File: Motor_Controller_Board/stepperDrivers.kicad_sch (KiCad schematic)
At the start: 17 parts, among them J401 Conn_01x04

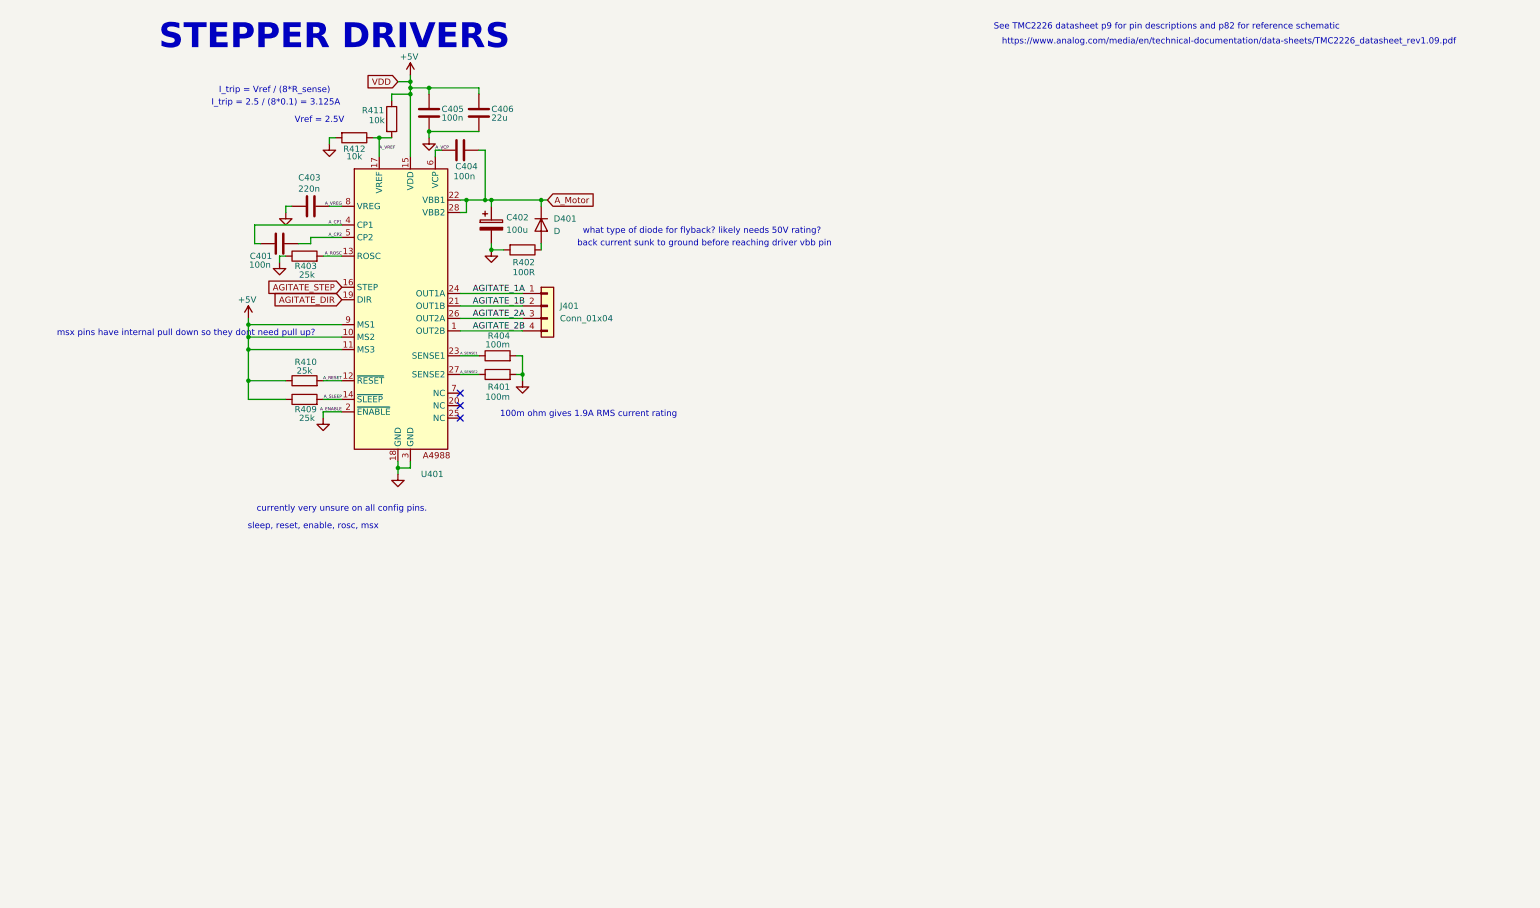
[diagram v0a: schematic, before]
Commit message: picking footprints. still need buck regulator footprints
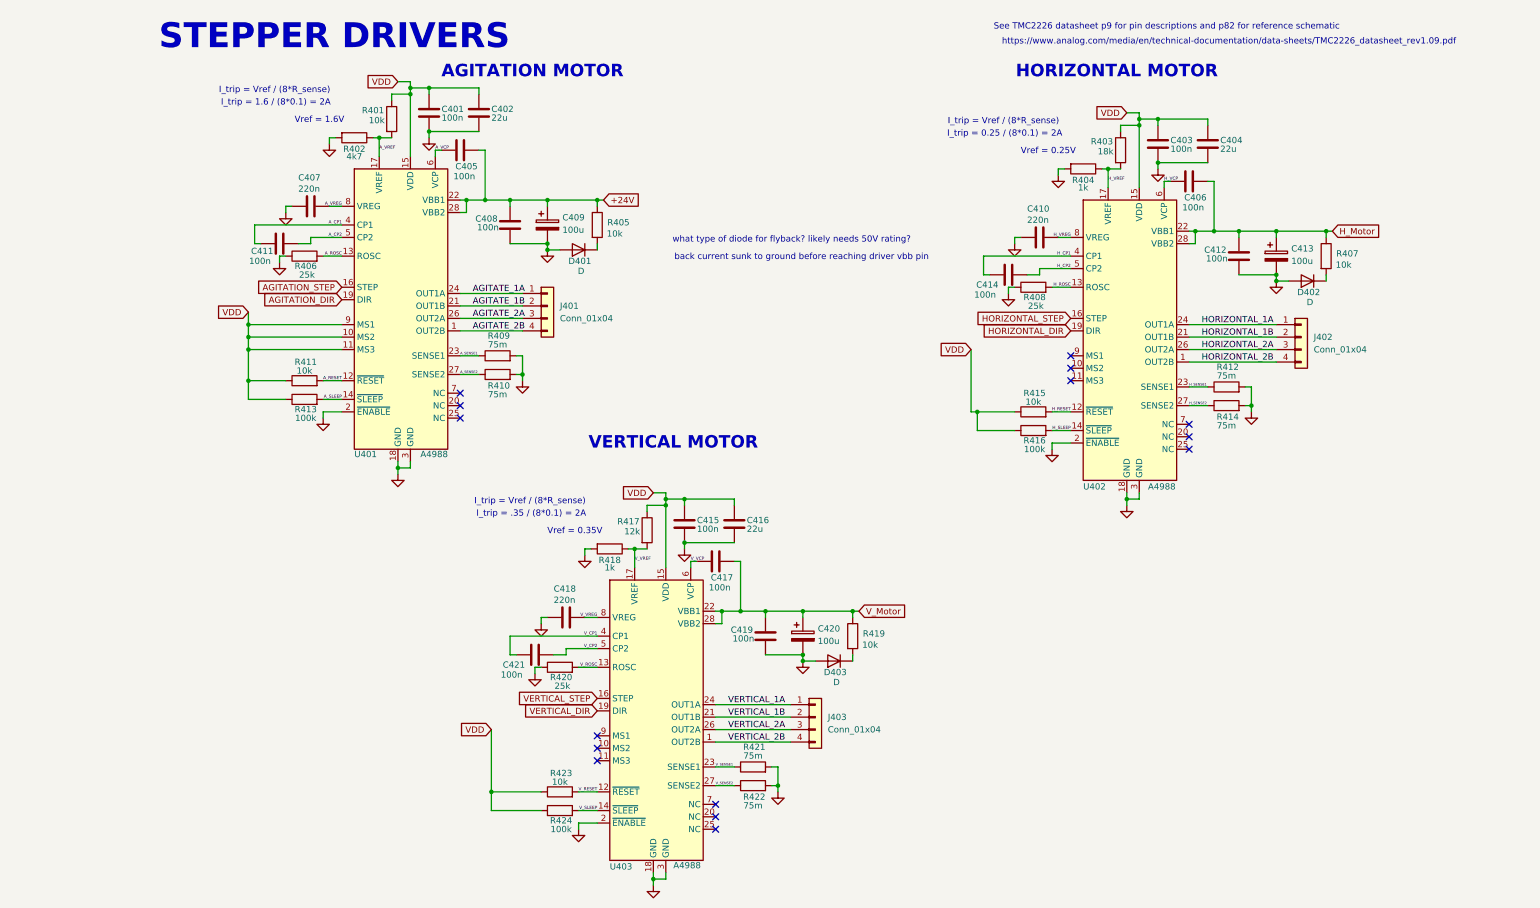
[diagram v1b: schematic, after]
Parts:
- removed C401: 100n, symbol Device:C
- removed R401: 100m, symbol Device:R
- added C404, C416: 22u, Capacitor_SMD:C_0603_1608Metric, symbol Device:C
- added C406, C408, C411, C412, C414, C415, C417, C419, C421: 100n, Capacitor_SMD:C_0603_1608Metric, symbol Device:C
- added C407, C410, C418: 220n, Capacitor_SMD:C_0805_2012Metric, symbol Device:C
- added C413, C420: 100u, Capacitor_THT:CP_Radial_D16.0mm_P7.50mm, symbol Device:C_Polarized
- added D402, D403: D, symbol Device:D
- added J402, J403: Conn_01x04, TerminalBlock:TerminalBlock_bornier-4_P5.08mm, symbol Connector_Generic:Conn_01x04
- added R403: 18k, Resistor_SMD:R_0603_1608Metric, symbol Device:R
- added R407, R415, R419, R423: 10k, Resistor_SMD:R_0603_1608Metric, symbol Device:R
- added R408, R420: 25k, Resistor_SMD:R_0603_1608Metric, symbol Device:R
- added R409, R410, R412, R414, R421, R422: 75m, Resistor_SMD:R_1206_3216Metric, symbol Device:R
- added R416, R424: 100k, Resistor_SMD:R_0603_1608Metric, symbol Device:R
- added R417: 12k, Resistor_SMD:R_0603_1608Metric, symbol Device:R
- added R418: 1k, Resistor_SMD:R_0603_1608Metric, symbol Device:R
- added U402, U403: A4988, Package_DFN_QFN:QFN-28-1EP_5x5mm_P0.5mm_EP3.25x3.25mm_ThermalVias, symbol a4988_symbol:A4988
- C401: renamed from C405; footprint (none) -> Capacitor_SMD:C_0603_1608Metric
- C402: renamed from C406; footprint (none) -> Capacitor_SMD:C_0603_1608Metric
- C403: value 220n -> 100n; footprint (none) -> Capacitor_SMD:C_0603_1608Metric
- C405: renamed from C404; footprint (none) -> Capacitor_SMD:C_0603_1608Metric; LCSC Part Number (none) -> C14663; MPN (none) -> CC0603KRX7R9BB104; Manufacturer (none) -> YAGEO
- C409: renamed from C402; footprint (none) -> Capacitor_THT:CP_Radial_D16.0mm_P7.50mm
- J401: footprint (none) -> TerminalBlock:TerminalBlock_bornier-4_P5.08mm
- R401: renamed from R411; footprint (none) -> Resistor_SMD:R_0603_1608Metric
- R402: renamed from R412; value 10k -> 4k7; footprint (none) -> Resistor_SMD:R_0603_1608Metric
- R404: value 100m -> 1k; footprint (none) -> Resistor_SMD:R_0603_1608Metric
- R405: renamed from R402; value 100R -> 10k; footprint (none) -> Resistor_SMD:R_0603_1608Metric
- R406: renamed from R403; footprint (none) -> Resistor_SMD:R_0603_1608Metric
- R411: renamed from R410; value 25k -> 10k; footprint (none) -> Resistor_SMD:R_0603_1608Metric
- R413: renamed from R409; value 25k -> 100k; footprint (none) -> Resistor_SMD:R_0603_1608Metric
- U401: value ~ -> A4988; footprint (none) -> Package_DFN_QFN:QFN-28-1EP_5x5mm_P0.5mm_EP3.25x3.25mm_ThermalVias
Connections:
- net A_CP1: now also C411.1
- net A_CP2: now also C411.2
- net A_SENSE1: now also R409.1; no longer R404.1
- net A_SENSE2: now also R410.1
- net A_VREG: now also C407.1; no longer C403.1
- net GND: now also D401.2 (A), C404.2, C407.2, C408.1, C410.2, C412.1, C413.2, C415.2, C416.2, C418.2, C419.1, C420.2, D402.2 (A), D403.2 (A), R408.1, R409.2, R410.2, R412.2, R414.2, R418.2, R420.1, R421.2, R422.2, U402.18 (GND), U402.2 (~{ENABLE}), U402.3 (GND), U403.18 (GND), U403.2 (~{ENABLE}), U403.3 (GND); no longer R405.2
- net +24V: now reaches R405.1
- net +24V: now also C405.2, C409.1, U401.22 (VBB1), U401.28 (VBB2), C408.2; no longer D401.2 (A)
- net +5V renamed VDD
- net VDD: now also C403.1, C404.1, C415.1, C416.1, R403.1, R415.1, R416.1, R417.1, R423.1, R424.1, U402.15 (VDD), U403.15 (VDD)
- net AGITATE_DIR renamed AGITATION_DIR
- net AGITATE_STEP renamed AGITATION_STEP
- removed net A_Motor: C405.2, C409.1, D401.1 (K), U401.22 (VBB1), U401.28 (VBB2)
- new net: D403.1 (K), R419.2
- new net: D401.1 (K), R405.2
- new net: D402.1 (K), R407.2
- new net HORIZONTAL_1A: J402.1 (Pin_1), U402.24 (OUT1A)
- new net HORIZONTAL_1B: J402.2 (Pin_2), U402.21 (OUT1B)
- new net HORIZONTAL_2A: J402.3 (Pin_3), U402.26 (OUT2A)
- new net HORIZONTAL_2B: J402.4 (Pin_4), U402.1 (OUT2B)
- new net HORIZONTAL_DIR: U402.19 (DIR)
- new net HORIZONTAL_STEP: U402.16 (STEP)
- new net H_CP1: C414.1, U402.4 (CP1)
- new net H_CP2: C414.2, U402.5 (CP2)
- new net H_Motor: C406.2, C412.2, C413.1, R407.1, U402.22 (VBB1), U402.28 (VBB2)
- new net H_RESET: R415.2, U402.12 (~{RESET})
- new net H_ROSC: R408.2, U402.13 (ROSC)
- new net H_SENSE1: R412.1, U402.23 (SENSE1)
- new net H_SENSE2: R414.1, U402.27 (SENSE2)
- new net H_SLEEP: R416.2, U402.14 (~{SLEEP})
- new net H_VCP: C406.1, U402.6 (VCP)
- new net H_VREF: R403.2, R404.1, U402.17 (VREF)
- new net H_VREG: C410.1, U402.8 (VREG)
- new net VERTICAL_1A: J403.1 (Pin_1), U403.24 (OUT1A)
- new net VERTICAL_1B: J403.2 (Pin_2), U403.21 (OUT1B)
- new net VERTICAL_2A: J403.3 (Pin_3), U403.26 (OUT2A)
- new net VERTICAL_2B: J403.4 (Pin_4), U403.1 (OUT2B)
- new net VERTICAL_DIR: U403.19 (DIR)
- new net VERTICAL_STEP: U403.16 (STEP)
- new net V_CP1: C421.1, U403.4 (CP1)
- new net V_CP2: C421.2, U403.5 (CP2)
- new net V_Motor: C417.2, C419.2, C420.1, R419.1, U403.22 (VBB1), U403.28 (VBB2)
- new net V_RESET: R423.2, U403.12 (~{RESET})
- new net V_ROSC: R420.2, U403.13 (ROSC)
- new net V_SENSE1: R421.1, U403.23 (SENSE1)
- new net V_SENSE2: R422.1, U403.27 (SENSE2)
- new net V_SLEEP: R424.2, U403.14 (~{SLEEP})
- new net V_VCP: C417.1, U403.6 (VCP)
- new net V_VREF: R417.2, R418.1, U403.17 (VREF)
- new net V_VREG: C418.1, U403.8 (VREG)
- no-connect marks 3 -> 15
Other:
- note added: "AGITATION MOTOR"
- note added: "HORIZONTAL MOTOR"
- note added: "I_trip = .35 / (8*0.1) = 2A"
- note added: "I_trip = 0.25 / (8*0.1) = 2A"
- note added: "I_trip = 1.6 / (8*0.1) = 2A"
- note added: "VERTICAL MOTOR"
- note added: "Vref = 0.25V"
- note added: "Vref = 0.35V"
- note added: "Vref = 1.6V"
- note removed: "100m ohm gives 1.9A RMS current rating"
- note removed: "I_trip = 2.5 / (8*0.1) = 3.125A"
- note removed: "Vref = 2.5V"
- note removed: "currently very unsure on all config pins."
- note removed: "msx pins have internal pull down so they dont need pull up?"
- note removed: "sleep, reset, enable, rosc, msx"
- moved on the sheet: C409, D401, R405

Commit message: schematic and footprints have been selected. ready to start layout, but always open to changes in schematic
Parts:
- C401, C403, C415: footprint Capacitor_SMD:C_0603_1608Metric -> Capacitor_SMD:C_0402_1005Metric; JCSC Part Number (none) -> C1525; MPN (none) -> CL05B104KO5NNNC; Manufacturer (none) -> Samsung Electro-Mechanics
- C402, C404, C416: JCSC Part Number (none) -> C45783; MPN (none) -> CL21A226MAQNNNE; Manufacturer (none) -> Samsung Electro-Mechanics
- C409, C413, C420: Manufacturer (none) -> Nichicon
- D401, D402, D403: value D -> IN5402; footprint (none) -> Diode_THT:D_DO-27_P15.24mm_Horizontal
- R401, R405, R407, R411, R415, R419, R423: JCSC Part Number (none) -> C25804; MPN (none) -> 0603WAF1002T5E; Manufacturer (none) -> UNI-ROYAL(Uniroyal Elec)
- R406, R408, R420: value 25k -> 24k; JCSC Part Number (none) -> C23352; MPN (none) -> 0603WAF2402T5E; Manufacturer (none) -> UNI-ROYAL(Uniroyal Elec)
- R413, R416, R424: JCSC Part Number (none) -> C25803; MPN (none) -> 0603WAF1003T5E; Manufacturer (none) -> UNI-ROYAL(Uniroyal Elec)
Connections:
- net GND: now also C401.1, C403.1, C415.1; no longer C401.2, C403.2, C415.2
- net VDD: now also C401.2, C403.2, C415.2; no longer C401.1, C403.1, C415.1

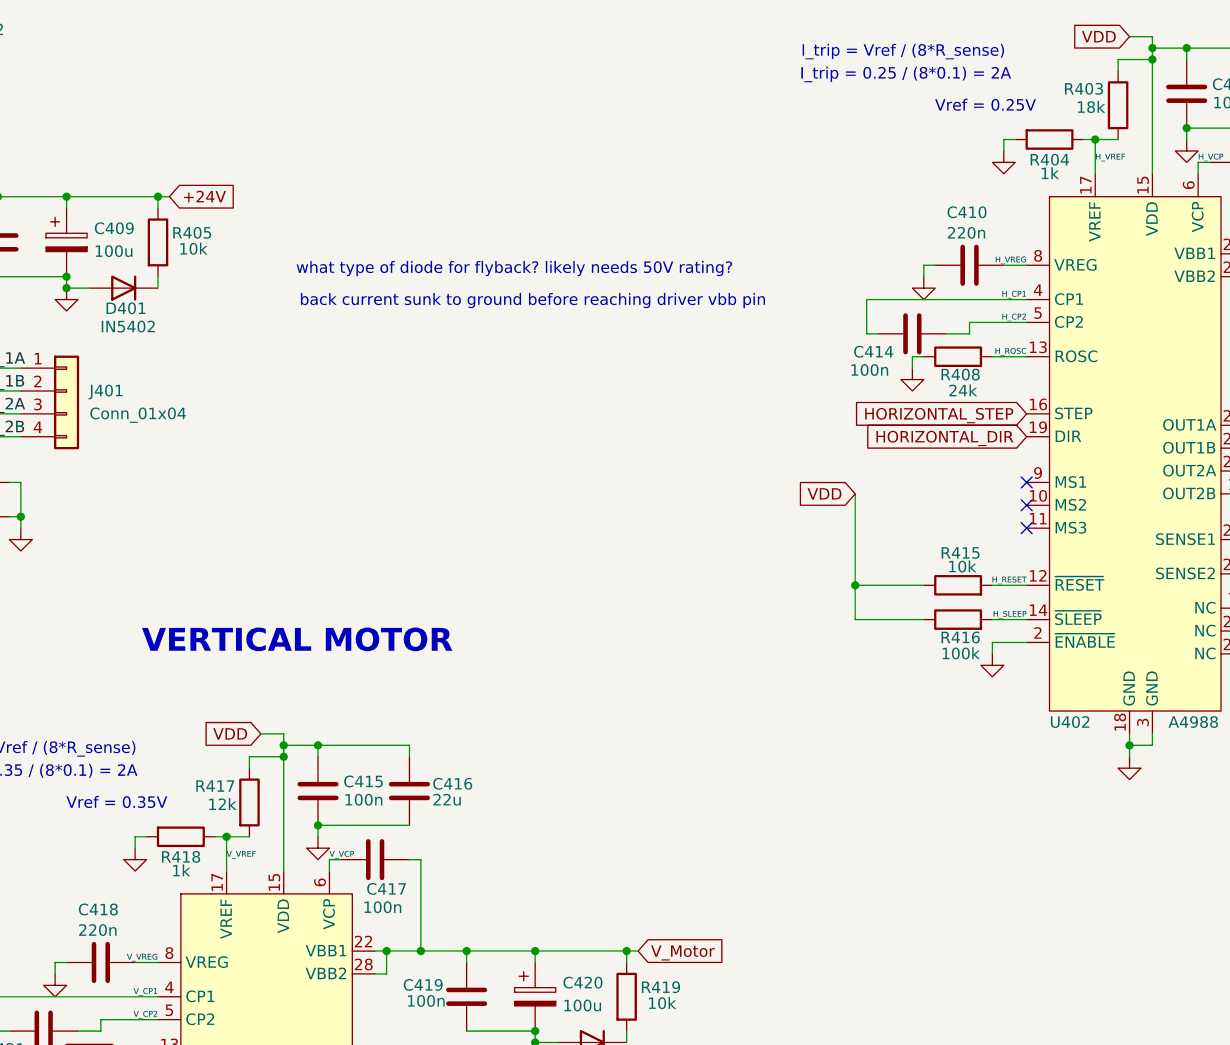
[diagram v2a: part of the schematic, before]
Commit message: changed jcsc to lcsc
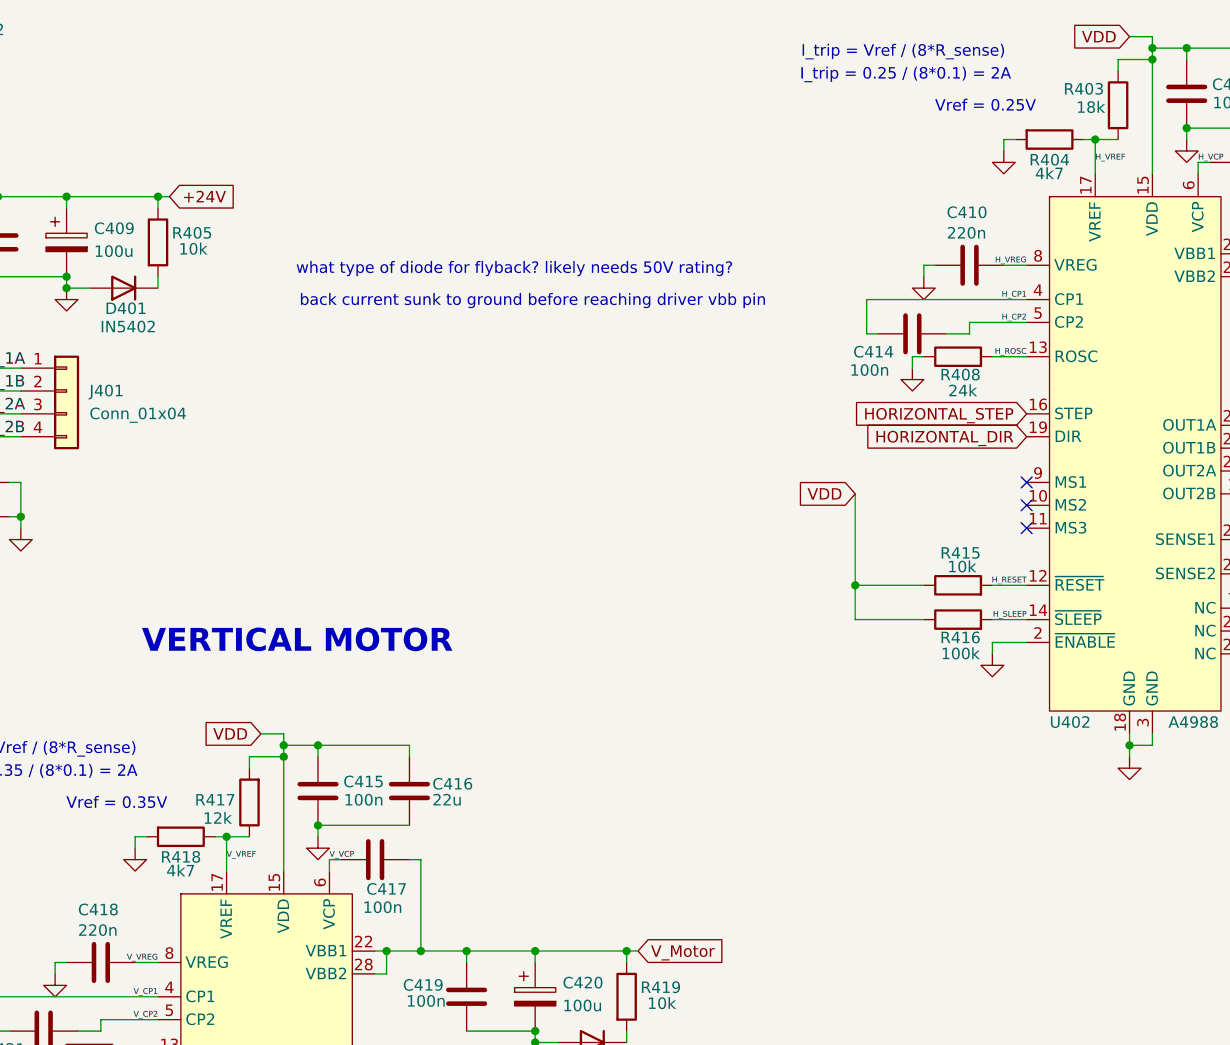
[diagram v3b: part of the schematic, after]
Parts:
- C401, C403, C415: JCSC Part Number C1525 -> (none); LCSC Part Number (none) -> C1525
- C402, C404, C416: JCSC Part Number C45783 -> (none); LCSC Part Number (none) -> C45783
- C409, C413, C420: Manufacturer Nichicon -> (none); now left out of the parts list
- D401, D402, D403, J401, J402, J403: now left out of the parts list
- R401, R405, R407, R411, R415, R419, R423: JCSC Part Number C25804 -> (none); LCSC Part Number (none) -> C25804
- R402: LCSC Part Number (none) -> C23162; MPN (none) -> 0603WAF4701T5E; Manufacturer (none) -> UNI-ROYAL(Uniroyal Elec)
- R403: LCSC Part Number (none) -> C25810; MPN (none) -> 0603WAF1802T5E; Manufacturer (none) -> UNI-ROYAL(Uniroyal Elec)
- R404, R418: value 1k -> 4k7; LCSC Part Number (none) -> C23162; MPN (none) -> 0603WAF4701T5E; Manufacturer (none) -> UNI-ROYAL(Uniroyal Elec)
- R406, R408, R420: JCSC Part Number C23352 -> (none); LCSC Part Number (none) -> C23352
- R413, R416, R424: JCSC Part Number C25803 -> (none); LCSC Part Number (none) -> C25803
- R417: LCSC Part Number (none) -> C22790; MPN (none) -> 0603WAF1202T5E; Manufacturer (none) -> UNI-ROYAL(Uniroyal Elec)
- U401, U402, U403: LCSC Part Number (none) -> C38437; MPN (none) -> A4988SETTR-T; Manufacturer (none) -> Allegro MicroSystems, LLC
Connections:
- net VDD: now also R417.2; no longer R417.1
- net V_VREF: now also R417.1; no longer R417.2
